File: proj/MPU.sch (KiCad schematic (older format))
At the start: 37 parts, among them J6 JLINK, U12 ATSAM4S16CA-AU, X2 12MHz

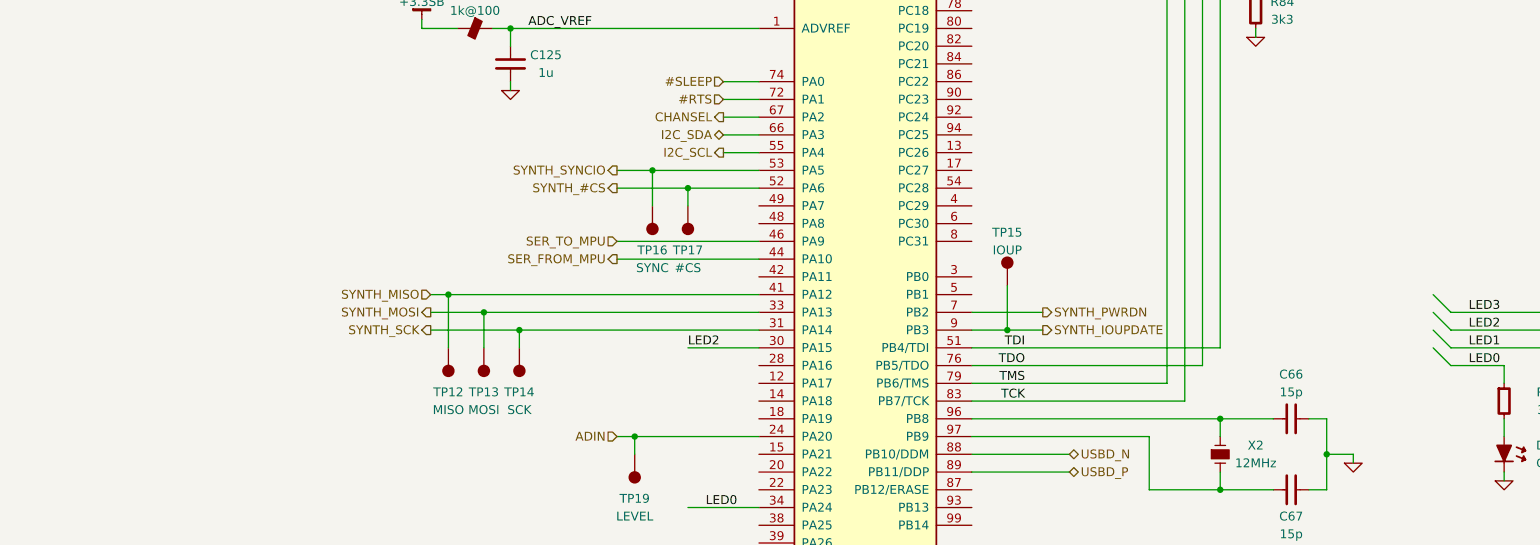
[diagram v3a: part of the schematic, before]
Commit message: Add SPI series resistors
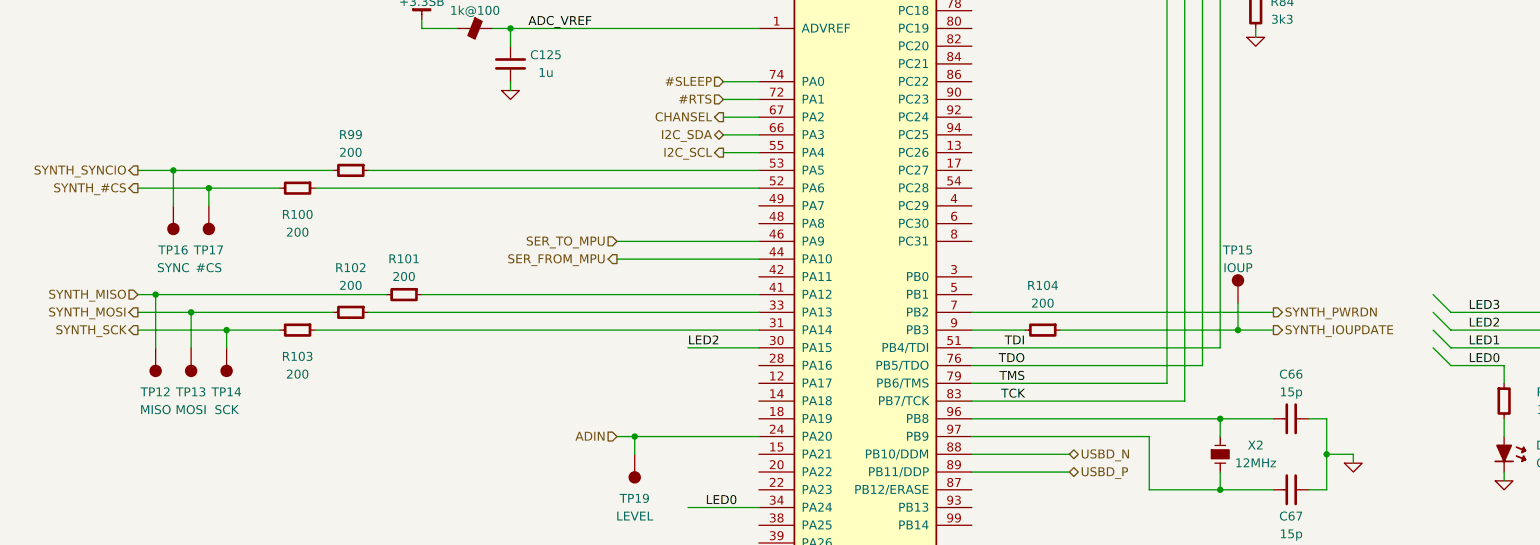
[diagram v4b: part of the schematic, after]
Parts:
- added R100, R101, R102, R103, R104, R99: 200, IPC7351-Nominal:RESC1608X50, symbol R-0603
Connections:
- net SYNTH_#CS: now also R100.2; no longer U12.52 (PA6)
- net SYNTH_IOUPDATE: now also R104.1; no longer U12.9 (PB3)
- net SYNTH_MISO: now also R101.2; no longer U12.41 (PA12)
- net SYNTH_MOSI: now also R102.2; no longer U12.33 (PA13)
- net SYNTH_SCK: now also R103.2; no longer U12.31 (PA14)
- net SYNTH_SYNCIO: now also R99.2; no longer U12.53 (PA5)
- new net: R103.1, U12.31 (PA14)
- new net: R102.1, U12.33 (PA13)
- new net: R101.1, U12.41 (PA12)
- new net: R100.1, U12.52 (PA6)
- new net: R99.1, U12.53 (PA5)
- new net: R104.2, U12.9 (PB3)
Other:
- moved on the sheet: TP12, TP13, TP14, TP15, TP16, TP17
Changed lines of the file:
@@
 	1    0    0    -1
 $EndComp
-Text HLabel 5400 4300 0    50   Output ~ 0
+Text HLabel 2700 4300 0    50   Output ~ 0
 SYNTH_#CS
 Wire Wire Line
-	5400 4300 6200 4300
-Text HLabel 7800 5100 2    50   Output ~ 0
+	2700 4300 3500 4300
+Text HLabel 9100 5100 2    50   Output ~ 0
 SYNTH_IOUPDATE
 Wire Wire Line
-	7400 5100 7800 5100
-Text HLabel 7800 5000 2    50   Output ~ 0
+	7900 5100 9100 5100
+Text HLabel 9100 5000 2    50   Output ~ 0
 SYNTH_PWRDN
 Wire Wire Line
-	7800 5000 7400 5000
+	9100 5000 7400 5000
 Text HLabel 6000 6800 0    50   Output ~ 0
 SYNTH_MRST
 Wire Wire Line
 	6000 6800 6200 6800
-Text HLabel 5400 4200 0    50   Output ~ 0
+Text HLabel 2700 4200 0    50   Output ~ 0
 SYNTH_SYNCIO
 Wire Wire Line
-	5400 4200 6200 4200
+	2700 4200 3800 4200
 Text HLabel 6000 3900 0    50   Output ~ 0
 CHANSEL
 Wire Wire Line
 	6200 3900 6000 3900
-Text HLabel 4350 5100 0    50   Output ~ 0
+Text HLabel 2700 5100 0    50   Output ~ 0
 SYNTH_SCK
 Wire Wire Line
-	4350 5100 6200 5100
-Text HLabel 4350 4900 0    50   Input ~ 0
+	2700 5100 3500 5100
+Text HLabel 2700 4900 0    50   Input ~ 0
 SYNTH_MISO
 Wire Wire Line
-	4350 4900 6200 4900
-Text HLabel 4350 5000 0    50   Output ~ 0
+	2700 4900 4100 4900
+Text HLabel 2700 5000 0    50   Output ~ 0
 SYNTH_MOSI
 Wire Wire Line
-	4350 5000 6200 5000
+	2700 5000 3800 5000
 Text HLabel 5400 5700 0    50   Input ~ 0
 ADIN
@@
 L TESTPOINT TP12
 U 1 1 54FCD6A4
-P 4450 5200
-F 0 "TP12" H 4450 5450 50  0000 C CNN
-F 1 "MISO" H 4450 5550 50  0000 C CNN
-F 2 "conn-test:TEST-SMD-SMALL" H 4450 5200 50  0001 C CNN
-F 3 "" H 4450 5200 50  0000 C CNN
-	1    4450 5200
+P 2800 5200
+F 0 "TP12" H 2800 5450 50  0000 C CNN
+F 1 "MISO" H 2800 5550 50  0000 C CNN
+F 2 "conn-test:TEST-SMD-SMALL" H 2800 5200 50  0001 C CNN
+F 3 "" H 2800 5200 50  0000 C CNN
+	1    2800 5200
 	1    0    0    1
 $EndComp
@@
 L TESTPOINT TP13
 U 1 1 54FCD80B
-P 4650 5200
-F 0 "TP13" H 4650 5450 50  0000 C CNN
-F 1 "MOSI" H 4650 5550 50  0000 C CNN
-F 2 "conn-test:TEST-SMD-SMALL" H 4650 5200 50  0001 C CNN
-F 3 "" H 4650 5200 50  0000 C CNN
-	1    4650 5200
+P 3000 5200
+F 0 "TP13" H 3000 5450 50  0000 C CNN
+F 1 "MOSI" H 3000 5550 50  0000 C CNN
+F 2 "conn-test:TEST-SMD-SMALL" H 3000 5200 50  0001 C CNN
+F 3 "" H 3000 5200 50  0000 C CNN
+	1    3000 5200
 	1    0    0    1
 $EndComp
@@
 L TESTPOINT TP14
 U 1 1 54FCD855
-P 4850 5200
-F 0 "TP14" H 4850 5450 50  0000 C CNN
-F 1 "SCK" H 4850 5550 50  0000 C CNN
-F 2 "conn-test:TEST-SMD-SMALL" H 4850 5200 50  0001 C CNN
-F 3 "" H 4850 5200 50  0000 C CNN
-	1    4850 5200
+P 3200 5200
+F 0 "TP14" H 3200 5450 50  0000 C CNN
+F 1 "SCK" H 3200 5550 50  0000 C CNN
+F 2 "conn-test:TEST-SMD-SMALL" H 3200 5200 50  0001 C CNN
+F 3 "" H 3200 5200 50  0000 C CNN
+	1    3200 5200
 	1    0    0    1
 $EndComp
 Wire Wire Line
-	4450 4900 4450 5200
-Connection ~ 4450 4900
-Wire Wire Line
-	4650 5200 4650 5000
-Connection ~ 4650 5000
-Wire Wire Line
-	4850 5200 4850 5100
-Connection ~ 4850 5100
+	2800 4900 2800 5200
+Connection ~ 2800 4900
+Wire Wire Line
+	3000 5000 3000 5200
+Connection ~ 3000 5000
+Wire Wire Line
+	3200 5100 3200 5200
+Connection ~ 3200 5100
 $Comp
 L TESTPOINT TP15
 U 1 1 54FCDF24
-P 7600 4850
-F 0 "TP15" H 7600 5150 50  0000 C CNN
-F 1 "IOUP" H 7600 5050 50  0000 C CNN
-F 2 "conn-test:TEST-SMD-SMALL" H 7600 4850 50  0001 C CNN
-F 3 "" H 7600 4850 50  0000 C CNN
-	1    7600 4850
-	1    0    0    -1
-$EndComp
-Wire Wire Line
-	7600 4850 7600 5100
-Connection ~ 7600 5100
+P 8900 4950
+F 0 "TP15" H 8900 5250 50  0000 C CNN
+F 1 "IOUP" H 8900 5150 50  0000 C CNN
+F 2 "conn-test:TEST-SMD-SMALL" H 8900 4950 50  0001 C CNN
+F 3 "" H 8900 4950 50  0000 C CNN
+	1    8900 4950
+	1    0    0    -1
+$EndComp
+Wire Wire Line
+	8900 4950 8900 5100
+Connection ~ 8900 5100
 $Comp
 L TESTPOINT TP16
 U 1 1 54FD0186
-P 5600 4400
-F 0 "TP16" H 5600 4650 50  0000 C CNN
-F 1 "SYNC" H 5600 4750 50  0000 C CNN
-F 2 "conn-test:TEST-SMD-SMALL" H 5600 4400 50  0001 C CNN
-F 3 "" H 5600 4400 50  0000 C CNN
-	1    5600 4400
+P 2900 4400
+F 0 "TP16" H 2900 4650 50  0000 C CNN
+F 1 "SYNC" H 2900 4750 50  0000 C CNN
+F 2 "conn-test:TEST-SMD-SMALL" H 2900 4400 50  0001 C CNN
+F 3 "" H 2900 4400 50  0000 C CNN
+	1    2900 4400
 	1    0    0    1
 $EndComp
@@
 L TESTPOINT TP17
 U 1 1 54FD01E4
-P 5800 4400
-F 0 "TP17" H 5800 4650 50  0000 C CNN
-F 1 "#CS" H 5800 4750 50  0000 C CNN
-F 2 "conn-test:TEST-SMD-SMALL" H 5800 4400 50  0001 C CNN
-F 3 "" H 5800 4400 50  0000 C CNN
-	1    5800 4400
+P 3100 4400
+F 0 "TP17" H 3100 4650 50  0000 C CNN
+F 1 "#CS" H 3100 4750 50  0000 C CNN
+F 2 "conn-test:TEST-SMD-SMALL" H 3100 4400 50  0001 C CNN
+F 3 "" H 3100 4400 50  0000 C CNN
+	1    3100 4400
 	1    0    0    1
 $EndComp
 Wire Wire Line
-	5800 4400 5800 4300
-Connection ~ 5800 4300
-Wire Wire Line
-	5600 4400 5600 4200
-Connection ~ 5600 4200
+	3100 4300 3100 4400
+Connection ~ 3100 4300
+Wire Wire Line
+	2900 4200 2900 4400
+Connection ~ 2900 4200
 $Comp
 L TESTPOINT TP19
@@
 Wire Wire Line
 	7700 2200 7400 2200
+$Comp
+L R-0603 R103
+U 1 1 54FF5C5A
+P 3600 5100
+F 0 "R103" V 3750 5100 50  0000 C CNN
+F 1 "200" V 3850 5100 50  0000 C CNN
+F 2 "IPC7351-Nominal:RESC1608X50" H 3600 5100 50  0001 C CNN
+F 3 "" H 3600 5150 60  0000 C CNN
+F 4 "Value" H 3600 5100 60  0001 C CNN "Manuf"
+F 5 "RES SMD 200 1% [0603]" H 4350 5650 60  0001 C CNN "BOM"
+	1    3600 5100
+	0    1    1    0
+$EndComp
+$Comp
+L R-0603 R102
+U 1 1 54FF5DD7
+P 3900 5000
+F 0 "R102" V 3650 5000 50  0000 C CNN
+F 1 "200" V 3750 5000 50  0000 C CNN
+F 2 "IPC7351-Nominal:RESC1608X50" H 3900 5000 50  0001 C CNN
+F 3 "" H 3900 5050 60  0000 C CNN
+F 4 "Value" H 3900 5000 60  0001 C CNN "Manuf"
+F 5 "RES SMD 200 1% [0603]" H 4650 5550 60  0001 C CNN "BOM"
+	1    3900 5000
+	0    1    1    0
+$EndComp
+$Comp
+L R-0603 R101
+U 1 1 54FF5EA9
+P 4200 4900
+F 0 "R101" V 4000 4900 50  0000 C CNN
+F 1 "200" V 4100 4900 50  0000 C CNN
+F 2 "IPC7351-Nominal:RESC1608X50" H 4200 4900 50  0001 C CNN
+F 3 "" H 4200 4950 60  0000 C CNN
+F 4 "Value" H 4200 4900 60  0001 C CNN "Manuf"
+F 5 "RES SMD 200 1% [0603]" H 4950 5450 60  0001 C CNN "BOM"
+	1    4200 4900
+	0    1    1    0
+$EndComp
+Wire Wire Line
+	4300 4900 6200 4900
+Wire Wire Line
+	6200 5000 4000 5000
+Wire Wire Line
+	6200 5100 3700 5100
+$Comp
+L R-0603 R100
+U 1 1 54FF695D
+P 3600 4300
+F 0 "R100" V 3750 4300 50  0000 C CNN
+F 1 "200" V 3850 4300 50  0000 C CNN
+F 2 "IPC7351-Nominal:RESC1608X50" H 3600 4300 50  0001 C CNN
+F 3 "" H 3600 4350 60  0000 C CNN
+F 4 "Value" H 3600 4300 60  0001 C CNN "Manuf"
+F 5 "RES SMD 200 1% [0603]" H 4350 4850 60  0001 C CNN "BOM"
+	1    3600 4300
+	0    1    1    0
+$EndComp
+$Comp
+L R-0603 R99
+U 1 1 54FF69E9
+P 3900 4200
+F 0 "R99" V 3700 4200 50  0000 C CNN
+F 1 "200" V 3800 4200 50  0000 C CNN
+F 2 "IPC7351-Nominal:RESC1608X50" H 3900 4200 50  0001 C CNN
+F 3 "" H 3900 4250 60  0000 C CNN
+F 4 "Value" H 3900 4200 60  0001 C CNN "Manuf"
+F 5 "RES SMD 200 1% [0603]" H 4650 4750 60  0001 C CNN "BOM"
+	1    3900 4200
+	0    1    1    0
+$EndComp
+Wire Wire Line
+	4000 4200 6200 4200
+Wire Wire Line
+	6200 4300 3700 4300
+$Comp
+L R-0603 R104
+U 1 1 54FF71D6
+P 7800 5100
+F 0 "R104" V 7550 5100 50  0000 C CNN
+F 1 "200" V 7650 5100 50  0000 C CNN
+F 2 "IPC7351-Nominal:RESC1608X50" H 7800 5100 50  0001 C CNN
+F 3 "" H 7800 5150 60  0000 C CNN
+F 4 "Value" H 7800 5100 60  0001 C CNN "Manuf"
+F 5 "RES SMD 200 1% [0603]" H 8550 5650 60  0001 C CNN "BOM"
+	1    7800 5100
+	0    1    1    0
+$EndComp
+Wire Wire Line
+	7700 5100 7400 5100
 $EndSCHEMATC

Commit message: Touchups
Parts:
- added TP21: CHANSEL, conn-test:TEST-SMD-SMALL, symbol TESTPOINT
- added TP22: ATTEN, conn-test:TEST-SMD-SMALL, symbol TESTPOINT
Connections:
- net ATTEN: now also TP22.1
- net CHANSEL: now also TP21.1
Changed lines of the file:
@@
 Wire Wire Line
 	2700 4200 3800 4200
-Text HLabel 6000 3900 0    50   Output ~ 0
+Text HLabel 5050 3900 0    50   Output ~ 0
 CHANSEL
 Wire Wire Line
-	6200 3900 6000 3900
+	5050 3900 6200 3900
 Text HLabel 2700 5100 0    50   Output ~ 0
 SYNTH_SCK
@@
 	5500 5800 5500 5700
 Connection ~ 5500 5700
-Text HLabel 7700 2900 2    50   Output ~ 0
+Text HLabel 7800 2900 2    50   Output ~ 0
 ATTEN
 Wire Wire Line
-	7700 2900 7400 2900
+	7800 2900 7400 2900
 Text HLabel 7700 3200 2    50   Output ~ 0
 PWRDN
@@
 Wire Wire Line
 	7700 5100 7400 5100
+$Comp
+L TESTPOINT TP21
+U 1 1 54FFB918
+P 5400 3850
+F 0 "TP21" H 5400 4200 50  0000 C CNN
+F 1 "CHANSEL" H 5400 4100 50  0000 C CNN
+F 2 "conn-test:TEST-SMD-SMALL" H 5400 3850 50  0001 C CNN
+F 3 "" H 5400 3850 50  0000 C CNN
+	1    5400 3850
+	1    0    0    -1
+$EndComp
+Wire Wire Line
+	5400 3850 5400 3900
+Connection ~ 5400 3900
+$Comp
+L TESTPOINT TP22
+U 1 1 54FFC7A3
+P 7700 2800
+F 0 "TP22" H 7700 3150 50  0000 C CNN
+F 1 "ATTEN" H 7700 3050 50  0000 C CNN
+F 2 "conn-test:TEST-SMD-SMALL" H 7700 2800 50  0001 C CNN
+F 3 "" H 7700 2800 50  0000 C CNN
+	1    7700 2800
+	1    0    0    -1
+$EndComp
+Wire Wire Line
+	7700 2800 7700 2900
+Connection ~ 7700 2900
 $EndSCHEMATC

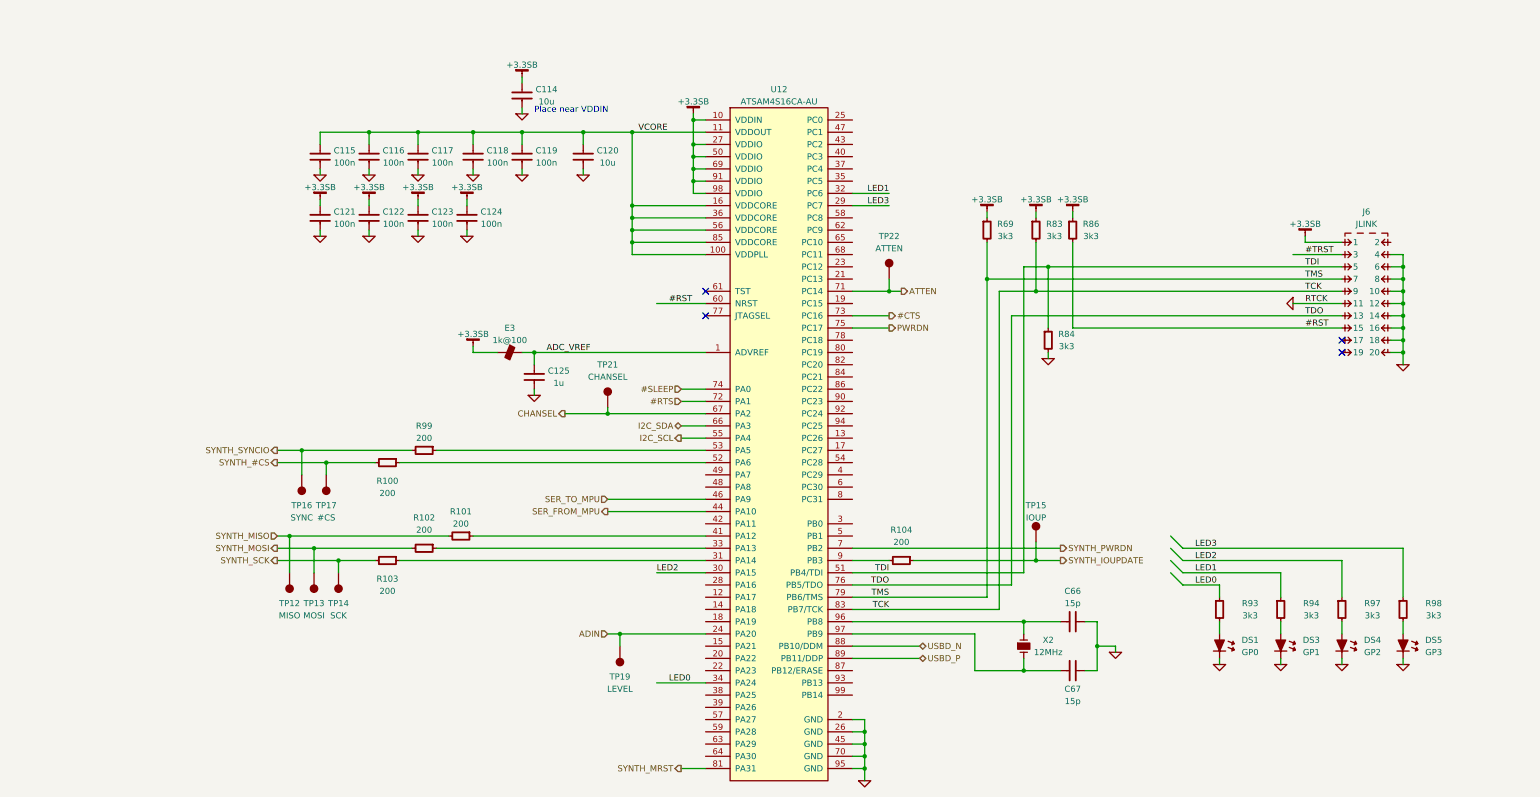
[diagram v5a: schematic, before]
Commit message: Add alternative MCU
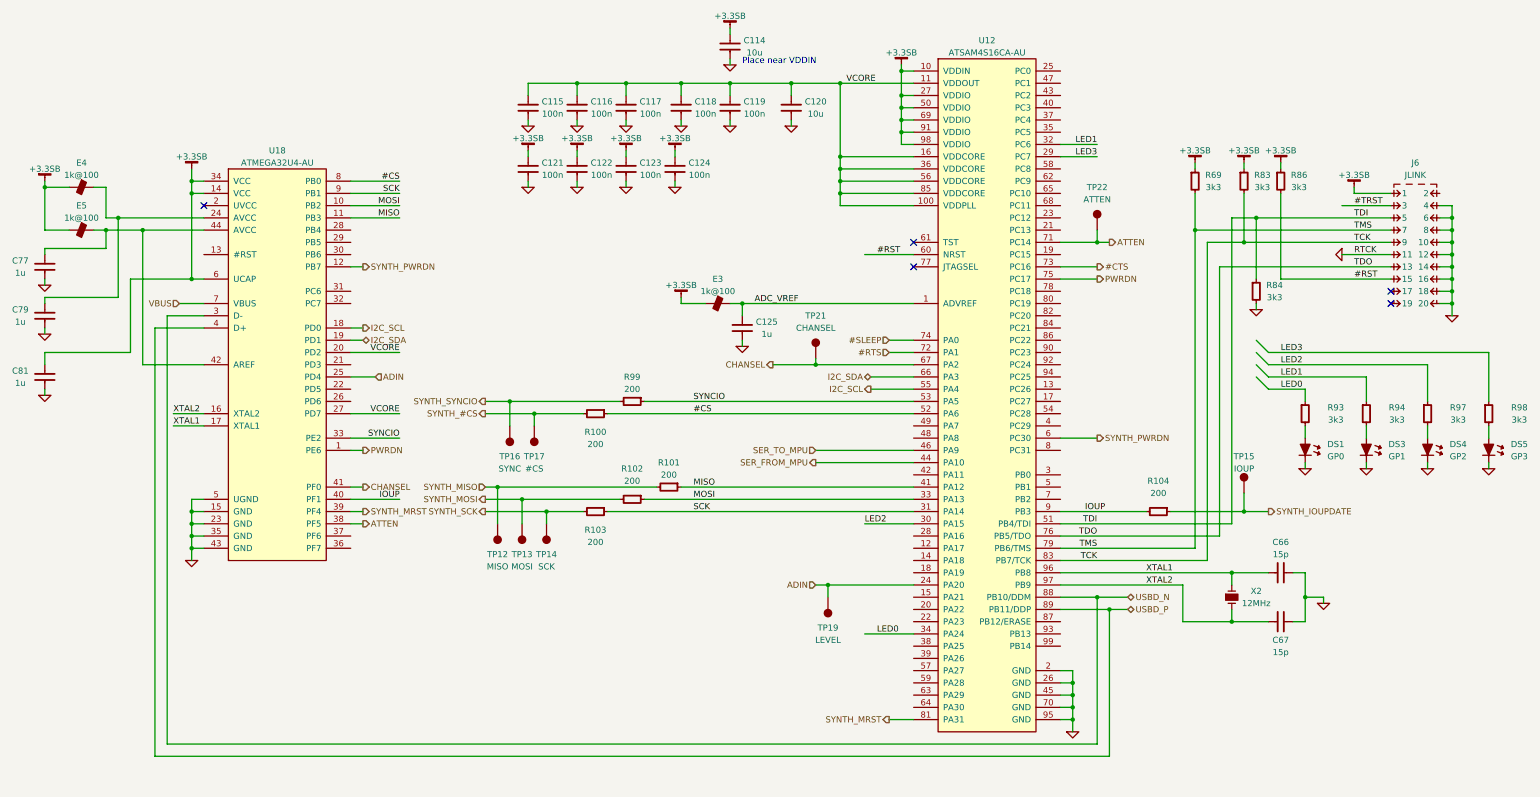
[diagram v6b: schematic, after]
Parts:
- added C77, C79, C81: 1u, IPC7351-Nominal:CAPC2012X70, symbol C-0805
- added E4, E5: 1k@100, IPC7351-Nominal:INDC1608X95, symbol BEAD-0603
- added U18: ATMEGA32U4-AU, IPC7351-Nominal:QFP80P1200X1200X120-44, symbol ATMEGA32U4-AU
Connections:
- net +3.3SB: now also C81.1, E4.1, E5.1, U18.14 (VCC), U18.34 (VCC), U18.6 (UCAP)
- net ADIN: now also U18.25 (PD4)
- net ATTEN: now also U18.38 (PF5)
- net CHANSEL: now also U18.41 (PF0)
- net GND: now also C77.2, C79.2, C81.2, U18.15 (GND), U18.23 (GND), U18.35 (GND), U18.43 (GND), U18.5 (UGND)
- net I2C_SCL: now also U18.18 (PD0)
- net I2C_SDA: now also U18.19 (PD1)
- net PWRDN: now also U18.1 (PE6)
- net SYNTH_MRST: now also U18.39 (PF4)
- net SYNTH_PWRDN: now also U12.6 (PC30), U18.12 (PB7); no longer U12.7 (PB2)
- net USBD_N: now also U18.3 (D-)
- net USBD_P: now also U18.4 (D+)
- net VCORE: now also U18.20 (PD2), U18.27 (PD7)
- net SCK: now reaches R103.1, U12.31 (PA14)
- net SCK: now also U18.9 (PB1)
- net MOSI: now reaches R102.1, U12.33 (PA13)
- net MOSI: now also U18.10 (PB2)
- net MISO: now reaches R101.1, U12.41 (PA12)
- net MISO: now also U18.11 (PB3)
- net #CS: now reaches R100.1, U12.52 (PA6)
- net #CS: now also U18.8 (PB0)
- net SYNCIO: now reaches R99.1, U12.53 (PA5)
- net SYNCIO: now also U18.33 (PE2)
- net IOUP: now reaches R104.2, U12.9 (PB3)
- net IOUP: now also U18.40 (PF1)
- net XTAL1: now reaches C66.2, U12.96 (PB8), X2.1
- net XTAL1: now also U18.17 (XTAL1)
- net XTAL2: now reaches C67.2, U12.97 (PB9), X2.2
- net XTAL2: now also U18.16 (XTAL2)
- new net: C79.1, E4.2, U18.24 (AVCC)
- new net: C77.1, E5.2, U18.42 (AREF), U18.44 (AVCC)
- new net VBUS: U18.7 (VBUS)
- no-connect marks 4 -> 5
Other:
- moved on the sheet: C114, C115, C116, C117, C118, C119, C120, C121, C122, C123, C124, C125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
